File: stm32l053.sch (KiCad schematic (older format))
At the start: 17 parts, among them P1 SWD, P2 CONN_01X23, P3 CONN_01X23, P4 BOOT0, P5 Ext Xtal, SW1 SW_PUSH, U1 STM32_LQFP64

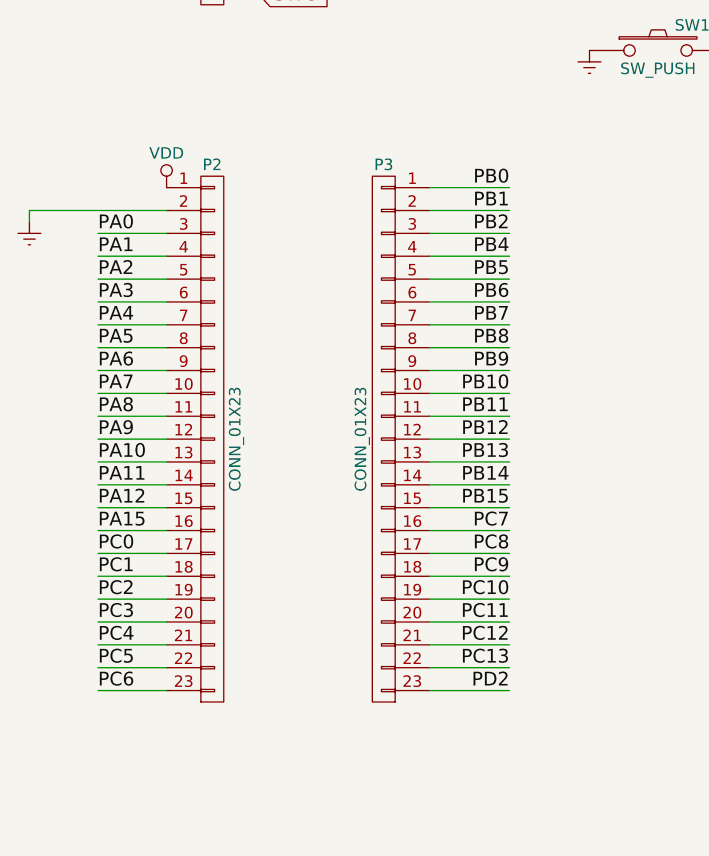
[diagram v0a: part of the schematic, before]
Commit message: Changing header layout to match pins on mcu
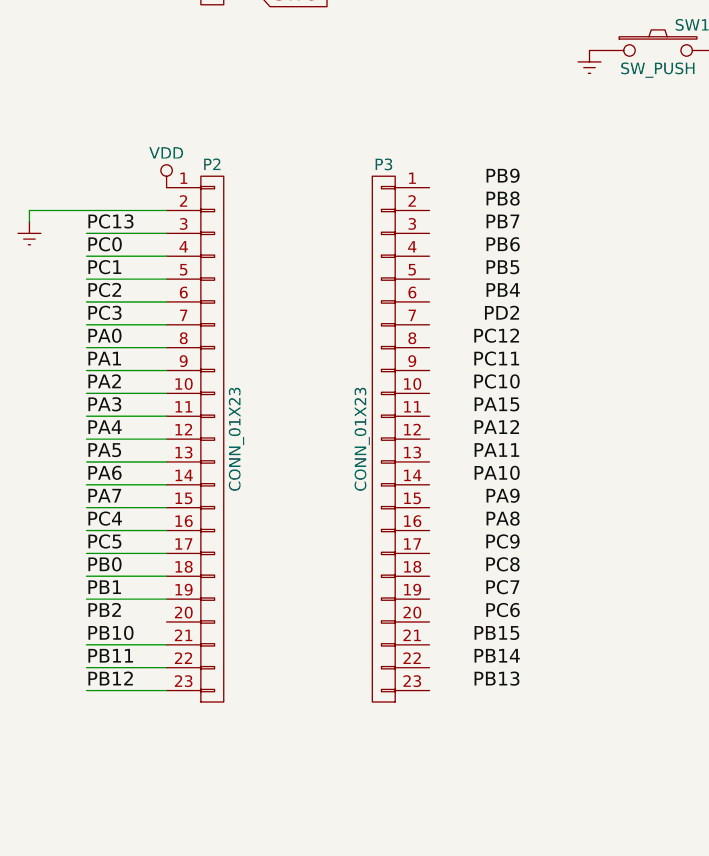
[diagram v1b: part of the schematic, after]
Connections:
- net PA0: now also P2.8 (P8); no longer P2.3 (P3)
- net PA1: now also P2.9 (P9); no longer P2.4 (P4)
- net PA10: no longer P2.13 (P13)
- net PA11: no longer P2.14 (P14)
- net PA12: no longer P2.15 (P15)
- net PA15: no longer P2.16 (P16)
- net PA2: now also P2.10 (P10); no longer P2.5 (P5)
- net PA3: now also P2.11 (P11); no longer P2.6 (P6)
- net PA4: now also P2.12 (P12); no longer P2.7 (P7)
- net PA5: now also P2.13 (P13); no longer P2.8 (P8)
- net PA6: now also P2.14 (P14); no longer P2.9 (P9)
- net PA7: now also P2.15 (P15); no longer P2.10 (P10)
- net PA8: no longer P2.11 (P11)
- net PA9: no longer P2.12 (P12)
- net PB0: now also P2.18 (P18); no longer P3.1 (P1)
- net PB1: now also P2.19 (P19); no longer P3.2 (P2)
- net PB10: now also P2.21 (P21); no longer P3.10 (P10)
- net PB11: now also P2.22 (P22); no longer P3.11 (P11)
- net PB12: now also P2.23 (P23); no longer P3.12 (P12)
- net PB13: no longer P3.13 (P13)
- net PB14: no longer P3.14 (P14)
- net PB15: no longer P3.15 (P15)
- net PB2: no longer P3.3 (P3)
- net PB4: no longer P3.4 (P4)
- net PB5: no longer P3.5 (P5)
- net PB6: no longer P3.6 (P6)
- net PB7: no longer P3.7 (P7)
- net PB8: no longer P3.8 (P8)
- net PB9: no longer P3.9 (P9)
- net PC0: now also P2.4 (P4); no longer P2.17 (P17)
- net PC1: now also P2.5 (P5); no longer P2.18 (P18)
- net PC10: no longer P3.19 (P19)
- net PC11: no longer P3.20 (P20)
- net PC12: no longer P3.21 (P21)
- net PC13: now also P2.3 (P3); no longer P3.22 (P22)
- net PC2: now also P2.6 (P6); no longer P2.19 (P19)
- net PC3: now also P2.7 (P7); no longer P2.20 (P20)
- net PC4: now also P2.16 (P16); no longer P2.21 (P21)
- net PC5: now also P2.17 (P17); no longer P2.22 (P22)
- net PC6: no longer P2.23 (P23)
- net PC7: no longer P3.16 (P16)
- net PC8: no longer P3.17 (P17)
- net PC9: no longer P3.18 (P18)
- net PD2: no longer P3.23 (P23)
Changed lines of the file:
@@
 Wire Wire Line
 	7550 6200 7050 6200
-Text Label 1200 2700 0    60   ~ 0
+Text Label 1150 3200 0    60   ~ 0
 PA0
-Text Label 1200 2800 0    60   ~ 0
+Text Label 1150 3300 0    60   ~ 0
 PA1
-Text Label 1200 2900 0    60   ~ 0
+Text Label 1150 3400 0    60   ~ 0
 PA2
-Text Label 1200 3000 0    60   ~ 0
+Text Label 1150 3500 0    60   ~ 0
 PA3
-Text Label 1200 3100 0    60   ~ 0
+Text Label 1150 3600 0    60   ~ 0
 PA4
-Text Label 1200 3200 0    60   ~ 0
+Text Label 1150 3700 0    60   ~ 0
 PA5
-Text Label 1200 3300 0    60   ~ 0
+Text Label 1150 3800 0    60   ~ 0
 PA6
-Text Label 1200 3400 0    60   ~ 0
+Text Label 1150 3900 0    60   ~ 0
 PA7
-Text Label 1200 3500 0    60   ~ 0
+Text Label 3050 4000 2    60   ~ 0
 PA8
-Text Label 1200 3600 0    60   ~ 0
+Text Label 3050 3900 2    60   ~ 0
 PA9
-Text Label 1200 3700 0    60   ~ 0
+Text Label 3050 3800 2    60   ~ 0
 PA10
-Text Label 1200 3800 0    60   ~ 0
+Text Label 3050 3700 2    60   ~ 0
 PA11
-Text Label 1200 3900 0    60   ~ 0
+Text Label 3050 3600 2    60   ~ 0
 PA12
-Wire Wire Line
-	1200 3900 1500 3900
-Wire Wire Line
-	1200 3800 1500 3800
-Wire Wire Line
-	1200 3700 1500 3700
-Wire Wire Line
-	1200 3600 1500 3600
-Wire Wire Line
-	1200 3500 1500 3500
-Wire Wire Line
-	1200 3400 1500 3400
-Wire Wire Line
-	1200 3300 1500 3300
-Wire Wire Line
-	1500 3200 1200 3200
-Wire Wire Line
-	1200 3100 1500 3100
-Wire Wire Line
-	1200 3000 1500 3000
-Wire Wire Line
-	1200 2900 1500 2900
-Wire Wire Line
-	1200 2800 1500 2800
-Wire Wire Line
-	1200 2700 1500 2700
 Text Label 6200 3700 0    60   ~ 0
 PA15
@@
 Wire Wire Line
 	6200 2200 6500 2200
-Text Label 1200 4000 0    60   ~ 0
+Text Label 3050 3500 2    60   ~ 0
 PA15
-Wire Wire Line
-	1200 4000 1500 4000
 Text Label 8800 2200 2    60   ~ 0
 PB0
@@
 Wire Wire Line
 	8450 3700 8800 3700
-Text Label 3000 2500 2    60   ~ 0
+Text Label 1150 4200 0    60   ~ 0
 PB0
-Text Label 3000 2600 2    60   ~ 0
+Text Label 1150 4300 0    60   ~ 0
 PB1
-Text Label 3000 2700 2    60   ~ 0
+Text Label 1150 4400 0    60   ~ 0
 PB2
-Wire Wire Line
-	2650 2500 3000 2500
-Wire Wire Line
-	2650 2600 3000 2600
-Wire Wire Line
-	2650 2700 3000 2700
-Text Label 3000 2800 2    60   ~ 0
+Text Label 3050 3000 2    60   ~ 0
 PB4
-Text Label 3000 2900 2    60   ~ 0
+Text Label 3050 2900 2    60   ~ 0
 PB5
-Text Label 3000 3000 2    60   ~ 0
+Text Label 3050 2800 2    60   ~ 0
 PB6
-Text Label 3000 3100 2    60   ~ 0
+Text Label 3050 2700 2    60   ~ 0
 PB7
-Text Label 3000 3200 2    60   ~ 0
+Text Label 3050 2600 2    60   ~ 0
 PB8
-Wire Wire Line
-	2650 2800 3000 2800
-Wire Wire Line
-	2650 2900 3000 2900
-Wire Wire Line
-	2650 3000 3000 3000
-Wire Wire Line
-	2650 3100 3000 3100
-Wire Wire Line
-	3000 3200 2650 3200
-Text Label 3000 3300 2    60   ~ 0
+Text Label 3050 2500 2    60   ~ 0
 PB9
-Text Label 3000 3400 2    60   ~ 0
+Text Label 1150 4500 0    60   ~ 0
 PB10
-Text Label 3000 3500 2    60   ~ 0
+Text Label 1150 4600 0    60   ~ 0
 PB11
-Text Label 3000 3600 2    60   ~ 0
+Text Label 1150 4700 0    60   ~ 0
 PB12
-Text Label 3000 3700 2    60   ~ 0
+Text Label 3050 4700 2    60   ~ 0
 PB13
-Text Label 3000 3800 2    60   ~ 0
+Text Label 3050 4600 2    60   ~ 0
 PB14
-Text Label 3000 3900 2    60   ~ 0
+Text Label 3050 4500 2    60   ~ 0
 PB15
-Wire Wire Line
-	2650 3300 3000 3300
-Wire Wire Line
-	2650 3400 3000 3400
-Wire Wire Line
-	2650 3500 3000 3500
-Wire Wire Line
-	2650 3600 3000 3600
-Wire Wire Line
-	2650 3700 3000 3700
-Wire Wire Line
-	2650 3800 3000 3800
-Wire Wire Line
-	2650 3900 3000 3900
 Wire Wire Line
 	5350 4400 6500 4400
@@
 Wire Wire Line
 	8450 4200 8800 4200
-Text Label 1200 4100 0    60   ~ 0
+Text Label 1150 2800 0    60   ~ 0
 PC0
-Text Label 1200 4200 0    60   ~ 0
+Text Label 1150 2900 0    60   ~ 0
 PC1
-Text Label 1200 4300 0    60   ~ 0
+Text Label 1150 3000 0    60   ~ 0
 PC2
-Text Label 1200 4500 0    60   ~ 0
+Text Label 1150 4000 0    60   ~ 0
 PC4
-Text Label 1200 4600 0    60   ~ 0
+Text Label 1150 4100 0    60   ~ 0
 PC5
-Text Label 1200 4700 0    60   ~ 0
+Text Label 3050 4400 2    60   ~ 0
 PC6
-Text Label 3000 4000 2    60   ~ 0
+Text Label 3050 4300 2    60   ~ 0
 PC7
-Text Label 3000 4100 2    60   ~ 0
+Text Label 3050 4200 2    60   ~ 0
 PC8
-Wire Wire Line
-	2650 4000 3000 4000
-Wire Wire Line
-	3000 4100 2650 4100
-Text Label 3000 4200 2    60   ~ 0
+Text Label 3050 4100 2    60   ~ 0
 PC9
-Text Label 3000 4300 2    60   ~ 0
+Text Label 3050 3400 2    60   ~ 0
 PC10
-Text Label 3000 4400 2    60   ~ 0
+Text Label 3050 3300 2    60   ~ 0
 PC11
-Text Label 3000 4500 2    60   ~ 0
+Text Label 3050 3200 2    60   ~ 0
 PC12
-Text Label 3000 4600 2    60   ~ 0
+Text Label 1150 2700 0    60   ~ 0
 PC13
-Wire Wire Line
-	2650 4200 3000 4200
-Wire Wire Line
-	2650 4300 3000 4300
-Wire Wire Line
-	2650 4400 3000 4400
-Wire Wire Line
-	2650 4500 3000 4500
-Wire Wire Line
-	2650 4600 3000 4600
-Text Label 1200 4400 0    60   ~ 0
+Text Label 1150 3100 0    60   ~ 0
 PC3
 Text Label 6200 3900 0    60   ~ 0
@@
 Wire Wire Line
 	6200 3900 6500 3900
-Text Label 3000 4700 2    60   ~ 0
+Text Label 3050 3100 2    60   ~ 0
 PD2
-$Comp
-L Earth #PWR013
-U 1 1 5803DE21
-P 900 2650
-F 0 "#PWR013" H 900 2400 50  0001 C CNN
-F 1 "Earth" H 900 2500 50  0001 C CNN
-F 2 "" H 900 2650 50  0000 C CNN
-F 3 "" H 900 2650 50  0000 C CNN
-	1    900  2650
-	1    0    0    -1
-$EndComp
 $Comp
 L VDD #PWR014
@@
 	-1   0    0    -1
 $EndComp
-Wire Wire Line
-	1200 4700 1500 4700
-Wire Wire Line
-	1200 4100 1500 4100
-Wire Wire Line
-	1200 4200 1500 4200
-Wire Wire Line
-	1200 4300 1500 4300
-Wire Wire Line
-	1500 4400 1200 4400
-Wire Wire Line
-	1200 4500 1500 4500
-Wire Wire Line
-	1500 4600 1200 4600
-Wire Wire Line
-	3000 4700 2650 4700
 Text GLabel 3700 1400 0    60   Input ~ 0
 BOOT0
@@
 Wire Wire Line
 	900  2600 1500 2600
+$Comp
+L Earth #PWR?
+U 1 1 5803D0EB
+P 900 2650
+F 0 "#PWR?" H 900 2400 50  0001 C CNN
+F 1 "Earth" H 900 2500 50  0001 C CNN
+F 2 "" H 900 2650 50  0000 C CNN
+F 3 "" H 900 2650 50  0000 C CNN
+	1    900  2650
+	1    0    0    -1
+$EndComp
+Wire Wire Line
+	1150 2700 1500 2700
+Wire Wire Line
+	1500 2800 1150 2800
+Wire Wire Line
+	1150 2900 1500 2900
+Wire Wire Line
+	1150 3000 1500 3000
+Wire Wire Line
+	1500 3100 1150 3100
+Wire Wire Line
+	1150 3200 1500 3200
+Wire Wire Line
+	1500 3300 1150 3300
+Wire Wire Line
+	1150 3400 1500 3400
+Wire Wire Line
+	1500 3500 1150 3500
+Wire Wire Line
+	1150 3600 1500 3600
+Wire Wire Line
+	1500 3700 1150 3700
+Wire Wire Line
+	1150 3800 1500 3800
+Wire Wire Line
+	1150 3900 1500 3900
+Wire Wire Line
+	1150 4000 1500 4000
+Wire Wire Line
+	1150 4100 1500 4100
+Wire Wire Line
+	1150 4200 1500 4200
+Wire Wire Line
+	1500 4300 1150 4300
+Wire Wire Line
+	1150 4500 1500 4500
+Wire Wire Line
+	1150 4600 1500 4600
+Wire Wire Line
+	1500 4700 1150 4700
 $EndSCHEMATC

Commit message: Simpler layout
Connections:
- net PA10: now also P3.14 (P14)
- net PA11: now also P3.13 (P13)
- net PA12: now also P3.12 (P12)
- net PA15: now also P3.11 (P11)
- net PA8: now also P3.16 (P16)
- net PA9: now also P3.15 (P15)
- net PB13: now also P3.23 (P23)
- net PB14: now also P3.22 (P22)
- net PB15: now also P3.21 (P21)
- net PB2: now also P2.20 (P20)
- net PB4: now also P3.6 (P6)
- net PB5: now also P3.5 (P5)
- net PB6: now also P3.4 (P4)
- net PB7: now also P3.3 (P3)
- net PB8: now also P3.2 (P2)
- net PB9: now also P3.1 (P1)
- net PC10: now also P3.10 (P10)
- net PC11: now also P3.9 (P9)
- net PC12: now also P3.8 (P8)
- net PC6: now also P3.20 (P20)
- net PC7: now also P3.19 (P19)
- net PC8: now also P3.18 (P18)
- net PC9: now also P3.17 (P17)
- net PD2: now also P3.7 (P7)
- net VLCD: now reaches C3.2, R2.2, U1.1 (VLCD)
- net VDD_USB: now reaches R3.2, U1.48 (VDD_USB)
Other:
- moved on the sheet: C3, P3
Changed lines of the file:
@@
 L C C3
 U 1 1 58032557
-P 6950 1650
-F 0 "C3" V 7100 1600 50  0000 L CNN
-F 1 "100nF" V 6800 1550 50  0000 L CNN
-F 2 "Capacitors_SMD:C_0805_HandSoldering" H 6988 1500 50  0001 C CNN
-F 3 "" H 6950 1650 50  0000 C CNN
-	1    6950 1650
+P 6850 1650
+F 0 "C3" V 7000 1600 50  0000 L CNN
+F 1 "100nF" V 6700 1550 50  0000 L CNN
+F 2 "Capacitors_SMD:C_0805_HandSoldering" H 6888 1500 50  0001 C CNN
+F 3 "" H 6850 1650 50  0000 C CNN
+	1    6850 1650
 	0    -1   -1   0
 $EndComp
@@
 	7350 950  7350 1900
 Wire Wire Line
-	7450 1900 7450 1750
-Wire Wire Line
-	7350 1750 7550 1750
-Connection ~ 7350 1750
-Wire Wire Line
-	7550 1750 7550 1900
-Connection ~ 7450 1750
+	7450 1150 7450 1900
+Wire Wire Line
+	7550 1150 7550 1900
 Wire Wire Line
 	7200 1150 7200 1900
@@
 Wire Wire Line
 	6700 1700 6700 1650
-Wire Wire Line
-	6700 1650 6800 1650
 Wire Wire Line
 	7100 1600 7100 1900
@@
 PD2
 $Comp
-L VDD #PWR014
+L VDD #PWR013
 U 1 1 5803DE79
 P 1500 2500
-F 0 "#PWR014" H 1500 2350 50  0001 C CNN
+F 0 "#PWR013" H 1500 2350 50  0001 C CNN
 F 1 "VDD" H 1500 2650 50  0000 C CNN
 F 2 "" H 1500 2500 50  0000 C CNN
@@
 L CONN_01X23 P3
 U 1 1 5803E381
-P 2450 3600
-F 0 "P3" H 2450 4800 50  0000 C CNN
-F 1 "CONN_01X23" V 2550 3600 50  0000 C CNN
-F 2 "Pin_Headers:Pin_Header_Straight_1x23" H 2450 3600 50  0001 C CNN
-F 3 "" H 2450 3600 50  0000 C CNN
-	1    2450 3600
-	-1   0    0    -1
+P 3250 3600
+F 0 "P3" H 3250 4800 50  0000 C CNN
+F 1 "CONN_01X23" V 3350 3600 50  0000 C CNN
+F 2 "Pin_Headers:Pin_Header_Straight_1x23" H 3250 3600 50  0001 C CNN
+F 3 "" H 3250 3600 50  0000 C CNN
+	1    3250 3600
+	1    0    0    -1
 $EndComp
 Text GLabel 3700 1400 0    60   Input ~ 0
@@
 $EndComp
 $Comp
-L Earth #PWR015
+L Earth #PWR014
 U 1 1 5803F003
 P 3350 1900
-F 0 "#PWR015" H 3350 1650 50  0001 C CNN
+F 0 "#PWR014" H 3350 1650 50  0001 C CNN
 F 1 "Earth" H 3350 1750 50  0001 C CNN
 F 2 "" H 3350 1900 50  0000 C CNN
@@
 NRST
 $Comp
-L Earth #PWR016
+L Earth #PWR015
 U 1 1 58039244
 P 9650 2100
-F 0 "#PWR016" H 9650 1850 50  0001 C CNN
+F 0 "#PWR015" H 9650 1850 50  0001 C CNN
 F 1 "Earth" H 9650 1950 50  0001 C CNN
 F 2 "" H 9650 2100 50  0000 C CNN
@@
 $EndComp
 $Comp
-L VDD #PWR017
+L VDD #PWR016
 U 1 1 5803924A
 P 9650 1800
-F 0 "#PWR017" H 9650 1650 50  0001 C CNN
+F 0 "#PWR016" H 9650 1650 50  0001 C CNN
 F 1 "VDD" H 9650 1950 50  0000 C CNN
 F 2 "" H 9650 1800 50  0000 C CNN
@@
 Connection ~ 9950 1350
 $Comp
-L Earth #PWR018
+L Earth #PWR017
 U 1 1 5803BDC8
 P 10700 1350
-F 0 "#PWR018" H 10700 1100 50  0001 C CNN
+F 0 "#PWR017" H 10700 1100 50  0001 C CNN
 F 1 "Earth" H 10700 1200 50  0001 C CNN
 F 2 "" H 10700 1350 50  0000 C CNN
@@
 	900  2600 1500 2600
 $Comp
-L Earth #PWR?
+L Earth #PWR018
 U 1 1 5803D0EB
 P 900 2650
-F 0 "#PWR?" H 900 2400 50  0001 C CNN
+F 0 "#PWR018" H 900 2400 50  0001 C CNN
 F 1 "Earth" H 900 2500 50  0001 C CNN
 F 2 "" H 900 2650 50  0000 C CNN
@@
 Wire Wire Line
 	1500 4700 1150 4700
+Wire Wire Line
+	1150 4400 1500 4400
+Text Label 7100 1900 1    60   ~ 0
+VLCD
+Wire Wire Line
+	7000 1650 7100 1650
+Text Label 7350 1900 1    60   ~ 0
+VDD
+Text Label 7800 1750 0    60   ~ 0
+VDD_USB
+Text Label 7450 1900 1    60   ~ 0
+VDD
+Text Label 7550 1900 1    60   ~ 0
+VDD
+Connection ~ 7450 1150
+Connection ~ 7550 1150
 $EndSCHEMATC
